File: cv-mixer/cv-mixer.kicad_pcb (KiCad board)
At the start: 2 copper layers, 72.5 x 128.5 mm, 39 parts, among them J1 Input A1, J10 Pot, J11 Input B3, J12 Pot, J13 Pot, J14 Output A, J15 Pot, J16 Output B, J18 Power, J19 Power, J2 Pot, J3 Input A2, J4 Pot, J5 Input A3, J6 Pot, J7 Input B1, J8 Pot, J9 Input B2, U1 TL072

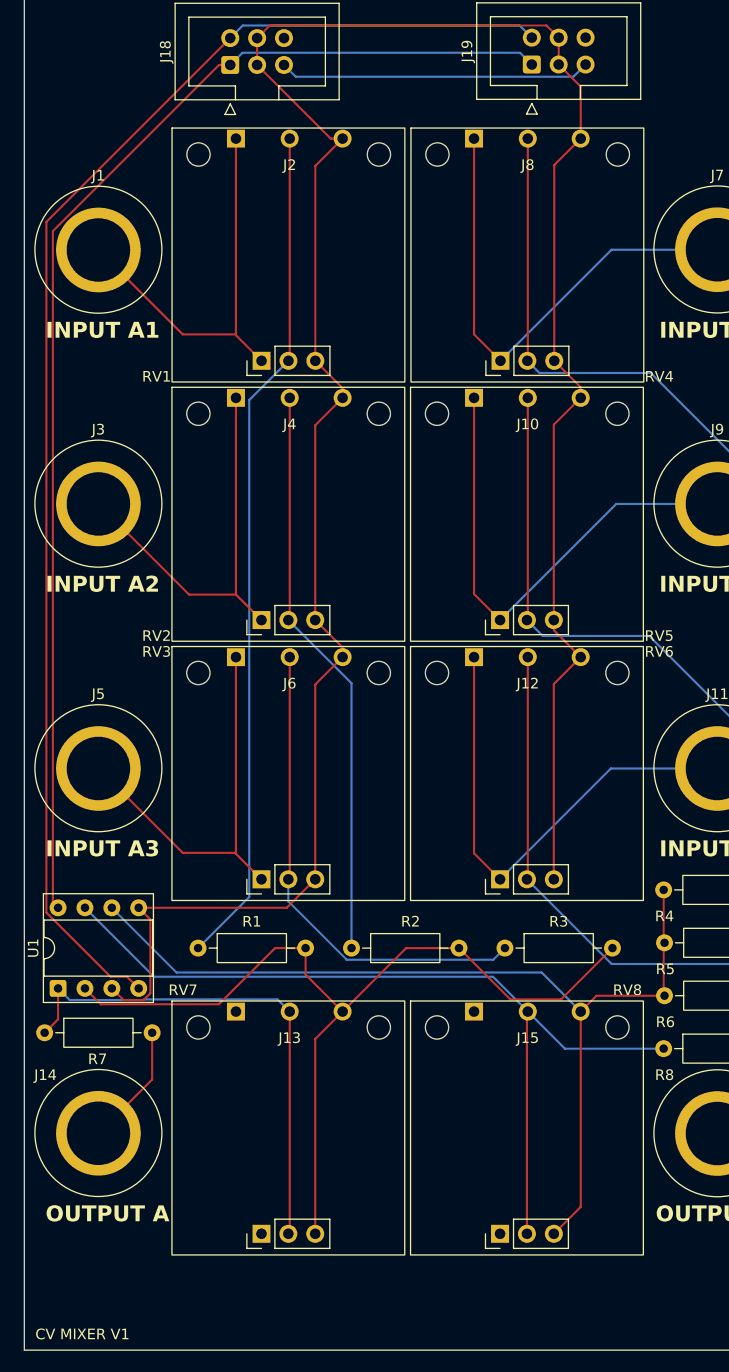
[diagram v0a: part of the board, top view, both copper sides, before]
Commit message: More space for backup pot
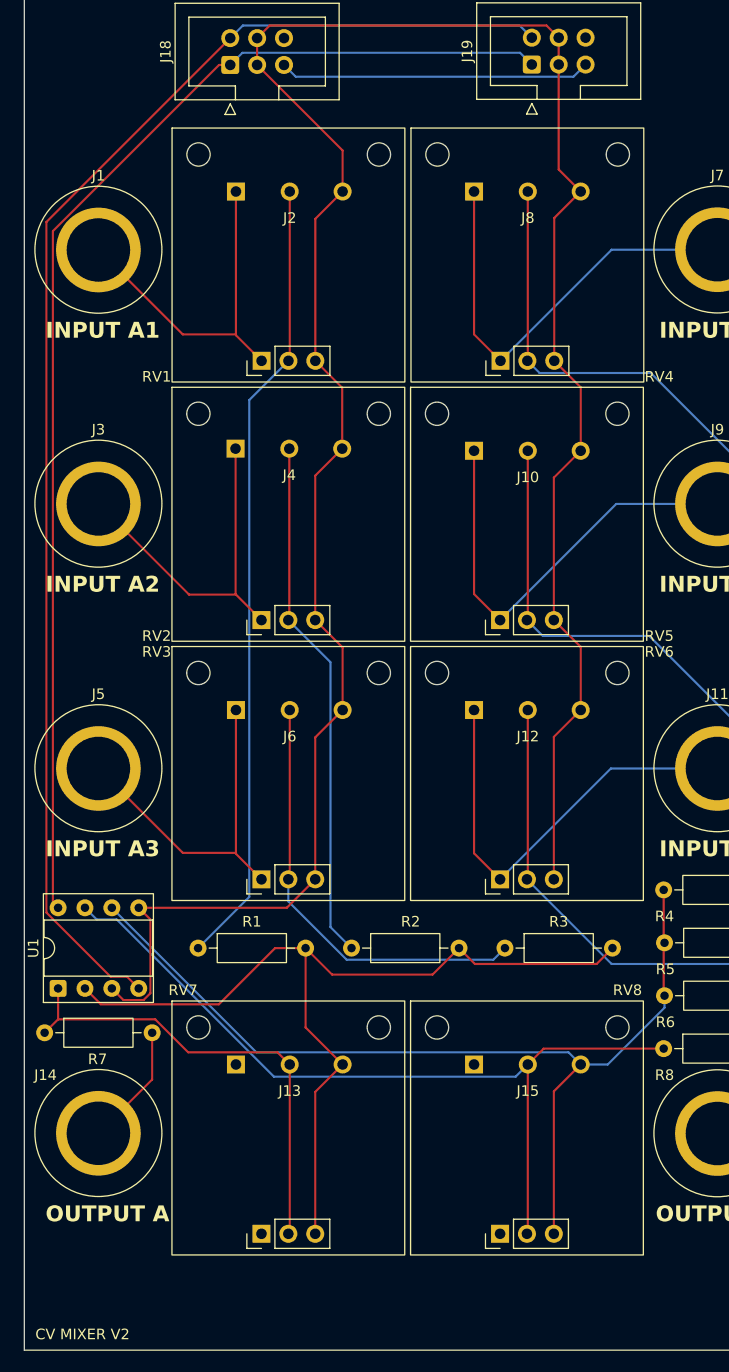
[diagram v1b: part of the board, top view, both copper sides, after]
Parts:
- moved J10 5.00 mm to (78.6, 69.0)
- moved J12 5.00 mm to (78.6, 93.5)
- moved J13 5.00 mm to (56.1, 127.0)
- moved J15 5.00 mm to (78.6, 127.0)
- moved J2 5.00 mm to (56.1, 44.5)
- moved J6 5.00 mm to (56.1, 93.5)
- moved J8 5.00 mm to (78.6, 44.5)
- moved J4 4.80 mm to (56.0, 68.8)
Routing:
- net Net-(J8-Pin_2): track 86.7 -> 81.7 mm
- net Net-(J7-Pin_1): track 46.9 -> 41.9 mm
- net Net-(J6-Pin_2): track 46.4 -> 41.4 mm
- net Net-(J2-Pin_2): track 80.1 -> 75.1 mm
- net Net-(J12-Pin_2): track 48.7 -> 43.7 mm
- net Net-(J11-Pin_1): track 46.9 -> 41.9 mm
- net Net-(J10-Pin_2): track 67.6 -> 62.6 mm
- net Net-(J10-Pin_1): track 47.1 -> 42.1 mm
- net Net-(J1-Pin_1): track 38.3 -> 33.3 mm
- net Net-(J5-Pin_1): track 38.3 -> 33.4 mm
- net Net-(J3-Pin_1): track 38.5 -> 33.8 mm
- net Net-(J4-Pin_2): track 54.5 -> 49.9 mm
- net Net-(J13-Pin_2): track 48.6 -> 44.4 mm
- net Net-(J15-Pin_2): track 81.2 -> 78.4 mm
- net GND: track 235.1 -> 234.4 mm
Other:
- board text added: "CV MIXER V2"
- board text removed: "CV MIXER V1"

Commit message: Various improvements
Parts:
- added C1: 100nF, Capacitor_THT:C_Disc_D4.3mm_W1.9mm_P5.00mm, F.Cu at (39.3, 106.4)
- added C2: 100nF, Capacitor_THT:C_Disc_D4.3mm_W1.9mm_P5.00mm, F.Cu at (44.7, 111.9)
- added G***: LOGO, modular2:ibis-small, F.Cu at (99.5, 146.0)
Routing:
- net GND: track 234.4 -> 240.7 mm
- net -12V: track 131.0 -> 133.9 mm
- net 12V: track 116.9 -> 117.6 mm

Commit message: Various fixes
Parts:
- added J17: Power, Connector_IDC:IDC-Header_2x03_P2.54mm_Vertical, F.Cu at (45.9, 20.0)
- moved J18 17.0 mm to (64.5, 20.0)
- moved J2 11.0 mm to (56.1, 33.5)
- moved J8 11.0 mm to (78.6, 33.5)
- moved J1 10.5 mm to (38.0, 36.5)
- moved J7 10.5 mm to (96.5, 36.5)
- moved RV1 10.5 mm to (55.0, 39.0)
- moved RV4 10.5 mm to (77.5, 39.0)
- moved J19 10.5 mm to (83.5, 20.0)
- moved F1 9.00 mm to (96.5, 20.5)
- moved F2 9.00 mm to (38.0, 20.5)
- moved J10 6.50 mm to (78.6, 62.5)
- moved J3 6.50 mm to (38.0, 64.5)
- moved J4 6.50 mm to (56.0, 62.3)
- moved J9 6.50 mm to (96.5, 64.5)
- moved RV2 6.50 mm to (55.0, 67.5)
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- renumbered F2 to F3, F2 to F4
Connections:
- J10 pad 1: Net-(J10-Pin_1) -> GND
- J10 pad 3: GND -> Net-(J10-Pin_3)
- J12 pad 1: Net-(J11-Pin_1) -> GND
- J12 pad 3: GND -> Net-(J11-Pin_1)
- J13 pad 1: unconnected-(J13-Pin_1-Pad1) -> Net-(J13-Pin_1)
- J13 pad 3: Net-(J13-Pin_3) -> unconnected-(J13-Pin_3-Pad3)
- J15 pad 1: unconnected-(J15-Pin_1-Pad1) -> Net-(J15-Pin_1)
- J15 pad 3: Net-(J15-Pin_3) -> unconnected-(J15-Pin_3-Pad3)
- J2 pad 1: Net-(J1-Pin_1) -> GND
- J2 pad 3: GND -> Net-(J1-Pin_1)
- J4 pad 1: Net-(J3-Pin_1) -> GND
- J4 pad 3: GND -> Net-(J3-Pin_1)
- J6 pad 1: Net-(J5-Pin_1) -> GND
- J6 pad 3: GND -> Net-(J5-Pin_1)
- J8 pad 1: Net-(J7-Pin_1) -> GND
- J8 pad 3: GND -> Net-(J7-Pin_1)
- J9 pad 1: Net-(J10-Pin_1) -> Net-(J10-Pin_3)
- R1 pad 2: Net-(J13-Pin_3) -> Net-(J13-Pin_1)
- R2 pad 2: Net-(J13-Pin_3) -> Net-(J13-Pin_1)
- R3 pad 2: Net-(J13-Pin_3) -> Net-(J13-Pin_1)
- R4 pad 2: Net-(J15-Pin_3) -> Net-(J15-Pin_1)
- R5 pad 2: Net-(J15-Pin_3) -> Net-(J15-Pin_1)
- R6 pad 2: Net-(J15-Pin_3) -> Net-(J15-Pin_1)
- RV1 pad 1: Net-(J1-Pin_1) -> GND
- RV1 pad 3: GND -> Net-(J1-Pin_1)
- RV2 pad 1: Net-(J3-Pin_1) -> GND
- RV2 pad 3: GND -> Net-(J3-Pin_1)
- RV3 pad 1: Net-(J5-Pin_1) -> GND
- RV3 pad 3: GND -> Net-(J5-Pin_1)
- RV4 pad 1: Net-(J7-Pin_1) -> GND
- RV4 pad 3: GND -> Net-(J7-Pin_1)
- RV5 pad 1: Net-(J10-Pin_1) -> GND
- RV5 pad 3: GND -> Net-(J10-Pin_3)
- RV6 pad 1: Net-(J11-Pin_1) -> GND
- RV6 pad 3: GND -> Net-(J11-Pin_1)
- RV7 pad 1: unconnected-(RV7-Pad1) -> Net-(J13-Pin_1)
- RV7 pad 3: Net-(J13-Pin_3) -> unconnected-(RV7-Pad3)
- RV8 pad 1: unconnected-(RV8-Pad1) -> Net-(J15-Pin_1)
- RV8 pad 3: Net-(J15-Pin_3) -> unconnected-(RV8-Pad3)
- U1 pad 2: Net-(J13-Pin_3) -> Net-(J13-Pin_1)
- U1 pad 6: Net-(J15-Pin_3) -> Net-(J15-Pin_1)
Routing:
- net Net-(J15-Pin_1): track 0.00 -> 99.8 mm
- net Net-(J15-Pin_3): track 88.8 -> 0.00 mm
- net Net-(J13-Pin_3): track 85.5 -> 0.00 mm
- net Net-(J13-Pin_1): track 0.00 -> 77.2 mm
- net Net-(J10-Pin_1): track 42.1 -> 0.00 mm
- net Net-(J10-Pin_3): track 0.00 -> 32.1 mm
- net GND: track 240.7 -> 260.4 mm
- net 12V: track 117.6 -> 135.5 mm
- net -12V: track 133.9 -> 151.0 mm
- net Net-(J2-Pin_2): track 75.1 -> 86.1 mm
- net 5V: track 29.4 -> 39.9 mm
- net Net-(J1-Pin_1): track 33.3 -> 43.1 mm
- net Net-(J11-Pin_1): track 41.9 -> 32.3 mm
- net Net-(J5-Pin_1): track 33.4 -> 42.4 mm
- net Net-(J7-Pin_1): track 41.9 -> 32.9 mm
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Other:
- board size 72.5 x 128.5 mm -> 72.5 x 137.5 mm

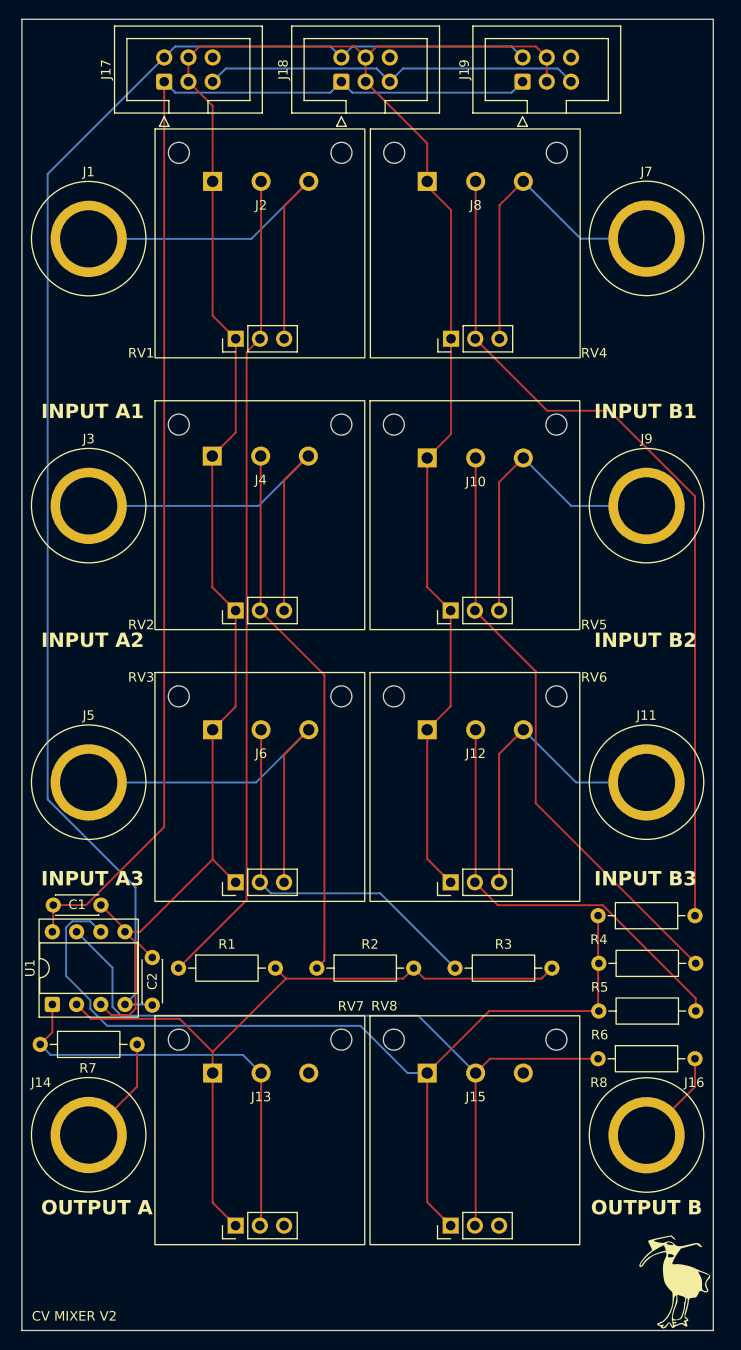
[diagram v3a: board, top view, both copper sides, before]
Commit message: Fix bug where cv mixer output was flipped
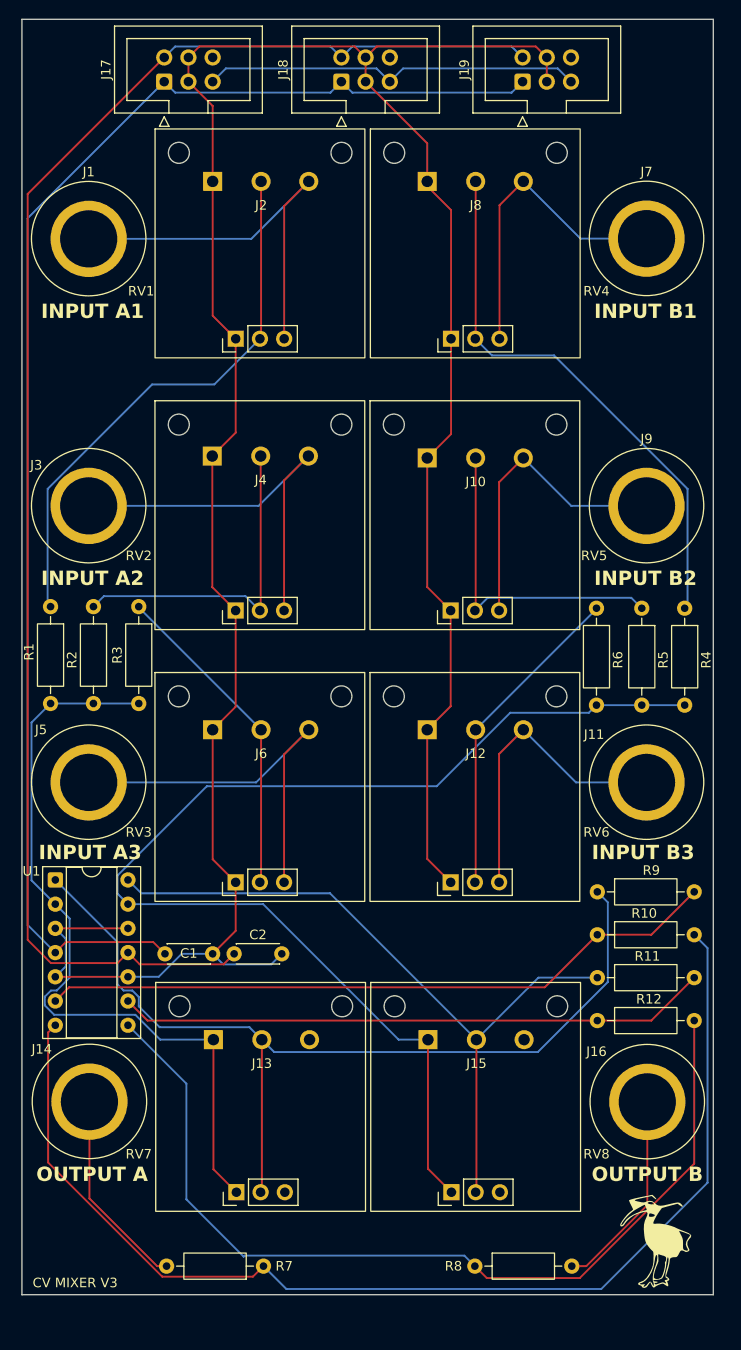
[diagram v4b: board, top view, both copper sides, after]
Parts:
- added R10: 100K, Resistor_THT:R_Axial_DIN0207_L6.3mm_D2.5mm_P10.16mm_Horizontal, F.Cu at (91.3, 109.5)
- added R11: 100K, Resistor_THT:R_Axial_DIN0207_L6.3mm_D2.5mm_P10.16mm_Horizontal, F.Cu at (91.3, 114.0)
- added R12: 100K, Resistor_THT:R_Axial_DIN0207_L6.3mm_D2.5mm_P10.16mm_Horizontal, F.Cu at (91.3, 118.5)
- added R9: 100K, Resistor_THT:R_Axial_DIN0207_L6.3mm_D2.5mm_P10.16mm_Horizontal, F.Cu at (91.3, 105.0)
- U1: value TL072 -> TL074; footprint Package_DIP:DIP-8_W7.62mm_Socket -> Package_DIP:DIP-14_W7.62mm_Socket
- moved R3 50.4 mm to (43.2, 75.1), turned to -90 degrees
- moved R2 44.6 mm to (38.5, 75.1), turned to -90 degrees
- moved R6 43.5 mm to (91.2, 75.3), turned to -90 degrees
- moved R1 40.2 mm to (34.0, 75.1), turned to -90 degrees
- moved R5 37.7 mm to (96.0, 75.3), turned to -90 degrees
- moved R7 33.0 mm to (56.3, 144.2), turned to 180 degrees
- moved R4 32.3 mm to (100.5, 75.3), turned to -90 degrees
- moved R8 25.3 mm to (78.5, 144.2)
- moved C2 13.6 mm to (58.2, 111.5), turned to 180 degrees
- moved U1 13.1 mm to (34.5, 103.8), turned to 0 degrees
- moved C1 12.8 mm to (51.0, 111.5)
- moved G*** 4.70 mm to (97.5, 141.8)
- moved J14 3.50 mm to (38.1, 127.0)
- moved F3 3.50 mm to (38.1, 140.0)
- moved F4 3.50 mm to (96.6, 140.0)
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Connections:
- R7 pad 1: Net-(J13-Pin_2) -> Net-(R10-Pad2)
- R8 pad 1: Net-(J15-Pin_2) -> Net-(R12-Pad2)
- U1 pad 4: -12V -> 12V
- U1 pad 6: Net-(J15-Pin_1) -> Net-(U1B--)
- U1 pad 7: Net-(J15-Pin_2) -> Net-(R10-Pad2)
- U1 pad 8: 12V -> Net-(R12-Pad2)
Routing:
- net Net-(R10-Pad2): track 0.00 -> 121.5 mm
- net Net-(R12-Pad2): track 0.00 -> 97.5 mm
- net Net-(U1B--): track 0.00 -> 71.7 mm
- net Net-(U1C--): track 0.00 -> 62.1 mm
- net Net-(J13-Pin_2): track 45.2 -> 97.6 mm
- net Net-(J8-Pin_2): track 90.4 -> 57.9 mm
- net Net-(J2-Pin_2): track 86.1 -> 57.8 mm
- net Net-(J10-Pin_2): track 62.6 -> 34.5 mm
- net Net-(J15-Pin_1): track 99.8 -> 124.7 mm
- net Net-(J4-Pin_2): track 56.9 -> 34.8 mm
- net GND: track 260.4 -> 276.7 mm
- net 12V: track 135.5 -> 150.4 mm
- net Net-(J12-Pin_2): track 45.6 -> 34.0 mm
- net Net-(J16-Pin_1): track 10.1 -> 21.4 mm
- net -12V: track 151.0 -> 162.0 mm
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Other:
- board size 72.5 x 137.5 mm -> 72.5 x 133.8 mm
- board text added: "CV MIXER V3"
- board text removed: "CV MIXER V2"

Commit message: More cv mixer updates
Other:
- board text added: "CV MIXER"
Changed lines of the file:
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@@
 		(layer "Edge.Cuts")
+	)
+	(gr_text "CV MIXER\nV3"
+		(at 35.25 16 0)
+		(layer "F.SilkS")
+		(effects
+			(font
+				(size 1 1)
+				(thickness 0.1)
+			)
+		)
 	)
 	(gr_text "INPUT A3"
@@
 		)
 	)
-	(gr_text "CV MIXER V3"
-		(at 36.58 146 0)
+	(gr_text "CV\nMIXER"
+		(at 37.75 142.5 0)
 		(layer "F.SilkS")
 		(effects
 			(font
-				(size 1 1)
-				(thickness 0.1)
+				(size 3 3)
+				(thickness 0.375)
 			)
 		)
